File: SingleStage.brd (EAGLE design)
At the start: 51.7 x 35.5 mm, 29 parts, among them T1 2N5089

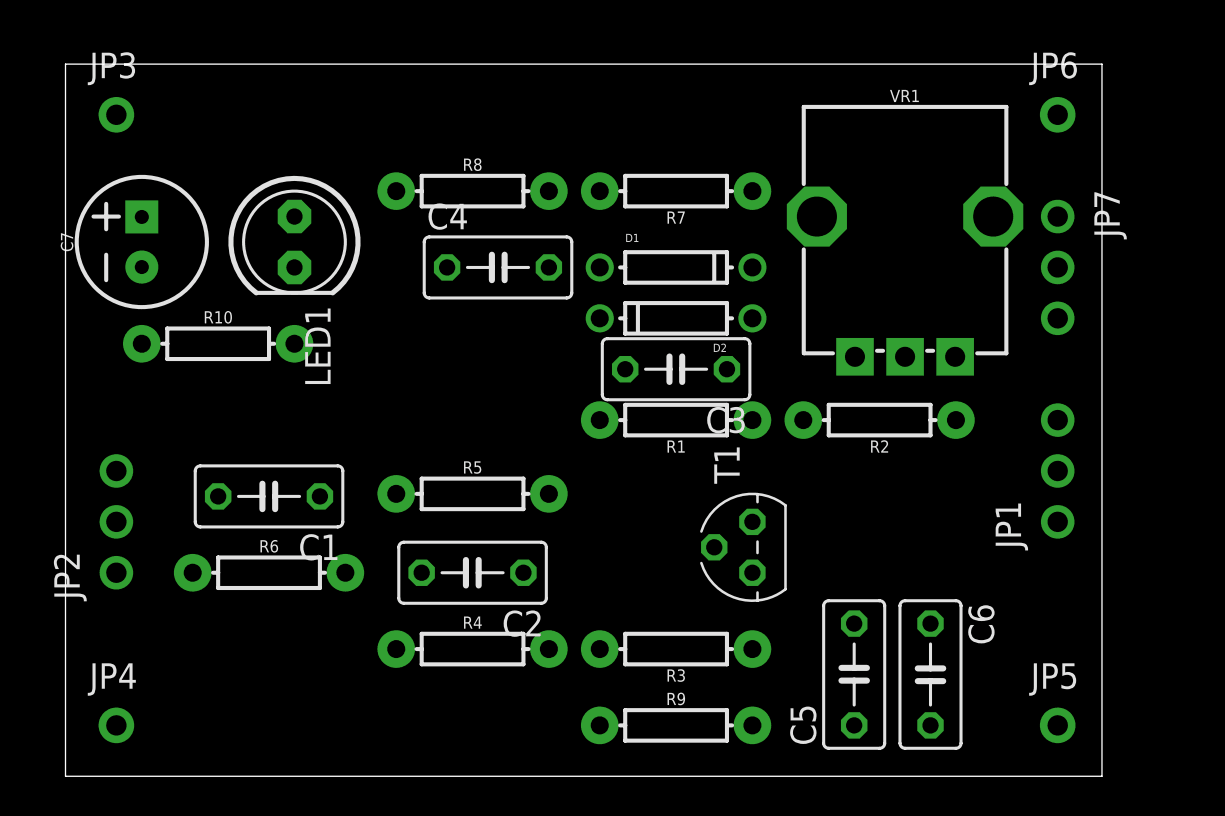
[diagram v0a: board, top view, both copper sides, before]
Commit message: Add files via upload
2-Layer board routed
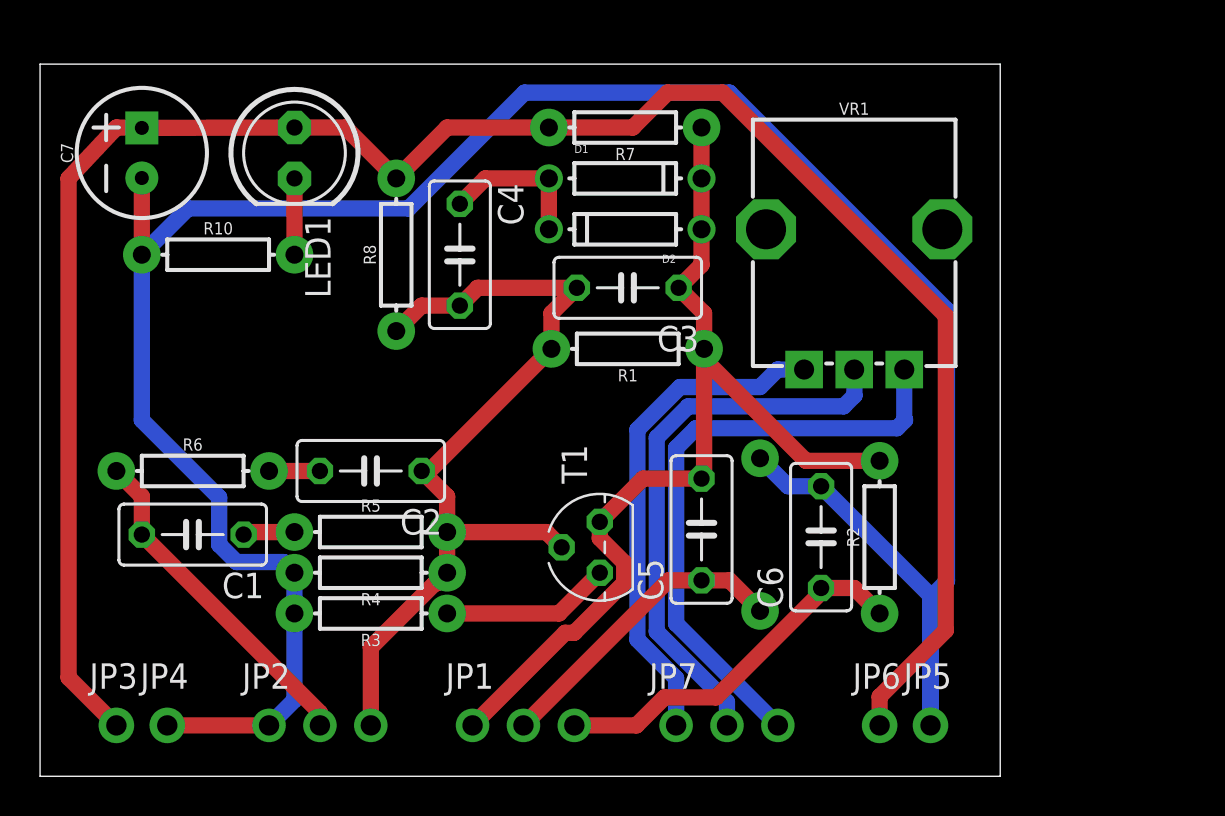
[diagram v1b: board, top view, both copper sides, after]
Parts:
- moved JP6 31.8 mm to (40.6, 2.54)
- moved JP3 30.5 mm to (2.54, 2.54)
- moved JP1 29.5 mm to (22.9, 2.54), turned to 0 degrees
- moved JP7 28.2 mm to (33.0, 2.54), turned to 0 degrees
- moved R3 15.3 mm to (15.2, 8.13)
- moved JP2 14.4 mm to (12.7, 2.54), turned to 0 degrees
- moved C5 10.5 mm to (31.8, 12.3)
- moved R9 10.4 mm to (34.7, 12.1), flipped to the bottom, turned to 270 degrees
- moved C6 8.77 mm to (37.7, 11.9), turned to 90 degrees
- moved T1 7.62 mm to (26.7, 11.4)
- moved C2 7.18 mm to (15.2, 15.2)
- moved JP5 6.35 mm to (43.2, 2.54)
- moved R4 6.35 mm to (15.2, 10.2), turned to 180 degrees
- moved R6 6.35 mm to (6.35, 15.2)
- moved R2 5.84 mm to (40.6, 11.9), turned to 90 degrees
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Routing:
- net GND: track 0.00 -> 124.4 mm
- net +9V: track 0.00 -> 102.4 mm
- net N$6: track 0.00 -> 50.4 mm
- net N$4: track 0.00 -> 43.4 mm
- net N$17: track 0.00 -> 30.5 mm
- net N$13: track 0.00 -> 27.9 mm
- net N$12: track 0.00 -> 25.1 mm
- net N$11: track 0.00 -> 18.7 mm
- net N$8: track 0.00 -> 16.9 mm
- net N$10: track 0.00 -> 15.4 mm
- net N$3: track 0.00 -> 8.46 mm
- net N$5: track 0.00 -> 7.51 mm
- net N$15: track 0.00 -> 3.81 mm
- net N$2: track 0.00 -> 2.59 mm
- net N$1: track 0.00 -> 2.54 mm
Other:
- board size 51.7 x 35.5 mm -> 47.9 x 35.5 mm

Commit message: Add files via upload
Layout complete ad Gerber files generated.
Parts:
- moved R2 5.97 mm to (46.6, 11.9)
- moved C6 5.59 mm to (43.3, 11.9)
- moved R9 5.21 mm to (39.9, 11.9), flipped to the top
- moved C2 5.08 mm to (20.2, 16.4)
- moved R5 5.03 mm to (20.2, 13.1)
- moved R4 4.98 mm to (20.2, 10.7)
- moved C3 4.95 mm to (33.0, 24.4)
- moved C4 4.95 mm to (24.6, 26.0)
- moved C5 4.95 mm to (36.7, 12.3)
- moved JP5 4.95 mm to (48.1, 2.54)
- moved JP6 4.95 mm to (45.6, 2.54)
- moved R1 4.95 mm to (33.0, 21.3)
- moved VR1 4.95 mm to (44.3, 27.3)
- moved C1 4.95 mm to (11.3, 12.1)
- moved R3 4.95 mm to (20.2, 8.13)
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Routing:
- net N$11: track 18.7 -> 20.0 mm
- net N$4: track 43.4 -> 44.4 mm
- added copper zone on layer 1, net +9V
- added copper zone on layer 16, net GND
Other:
- board size 47.9 x 35.5 mm -> 55.9 x 35.6 mm
- board text added: "BASE"
- board text added: "COL"
- board text added: "Fuzz-Stage-V1 201904"
- board text added: "GND"
- board text added: "HP"
- board text added: "LP"
- board text added: "SN:"
- board text added: "T1"
- board text added: "T2"
- board text added: "VIN"
- board text added: "W"
